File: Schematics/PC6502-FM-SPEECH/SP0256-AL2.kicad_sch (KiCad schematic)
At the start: 16 parts, among them U5 SP0256-AL2, U6 MCP6002-xSN, X2 CXO_DIP8

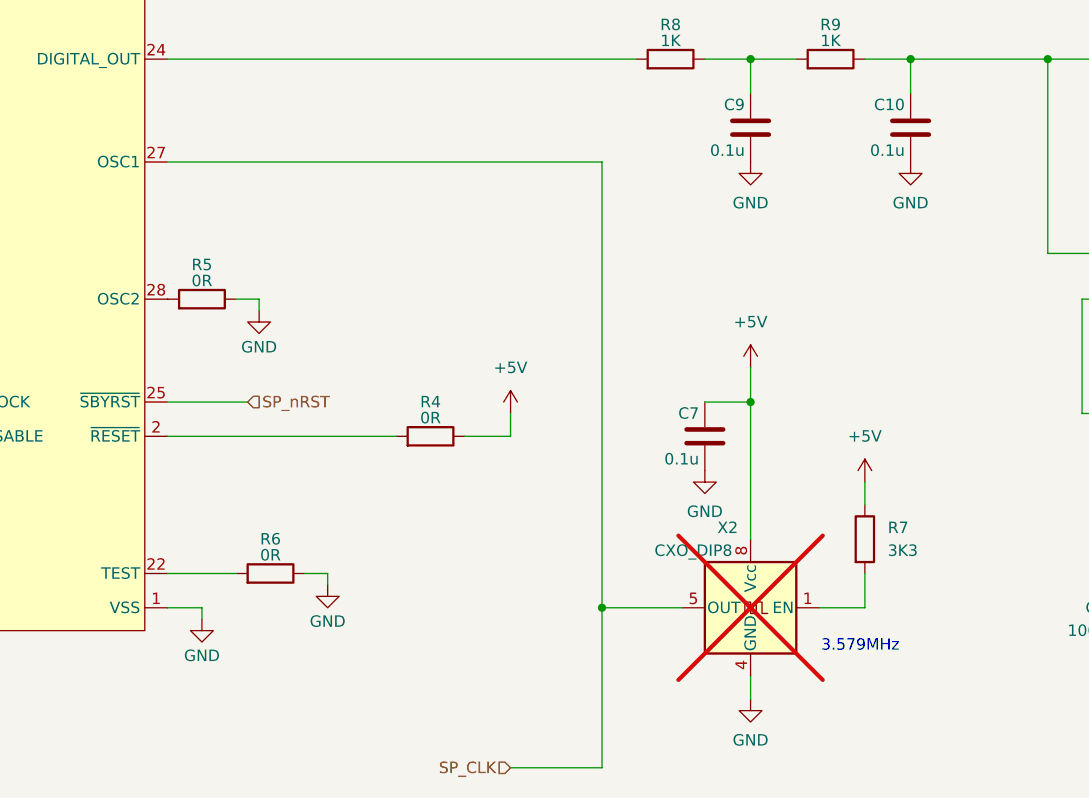
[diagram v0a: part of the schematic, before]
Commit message: Ordered Storage, FM/Speech, Dual SPI and APPLE II slot PCBs
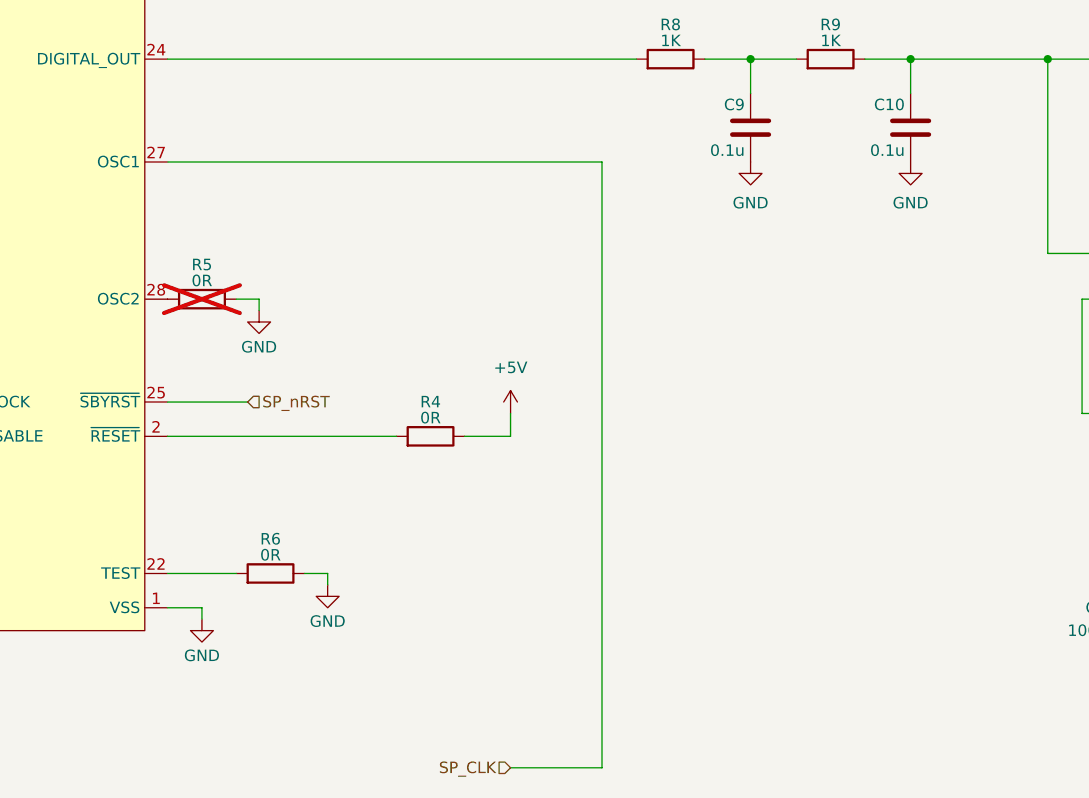
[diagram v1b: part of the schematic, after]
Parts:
- removed C7: 0.1u, Capacitor_SMD:C_0603_1608Metric, symbol Device:C
- removed R7: 3K3, Resistor_SMD:R_0603_1608Metric_Pad0.98x0.95mm_HandSolder, symbol Device:R
- removed X2: CXO_DIP8, Oscillator:Oscillator_DIP-8, symbol Oscillator:CXO_DIP8
- R5: now not fitted
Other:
- note removed: "3.579MHz"

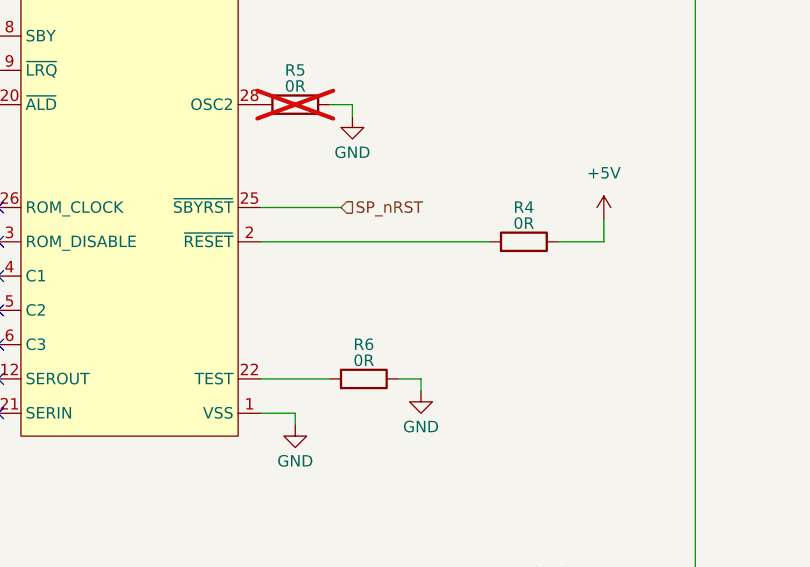
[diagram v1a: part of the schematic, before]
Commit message: SP0256 Speech synth working
SP0256 now working, couple of extra wires needed, but PCB and schematics updated.
Test code (SP0256_TEST3.BAS) created.
CPLD updated.
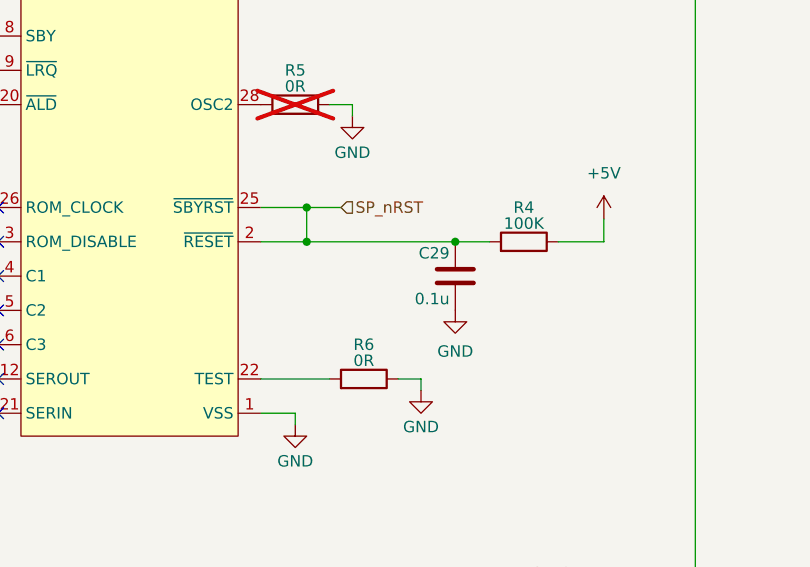
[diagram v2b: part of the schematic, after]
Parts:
- added C29: 0.1u, Capacitor_SMD:C_0603_1608Metric, symbol Device:C
- R4: value 0R -> 100K
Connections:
- net GND: now also C29.2
- net SP_nRST: now also R4.2, U5.2 (~{RESET}), C29.1
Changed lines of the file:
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@@
+	)
+	(junction
+		(at 110.49 113.03)
+		(diameter 0)
+		(color 0 0 0 0)
 	)
 	(junction
@@
 	)
 	(junction
+		(at 110.49 116.84)
+		(diameter 0)
+		(color 0 0 0 0)
+	)
+	(junction
 		(at 121.92 59.69)
 		(diameter 0)
@@
 	)
 	(junction
+		(at 127 116.84)
+		(diameter 0)
+		(color 0 0 0 0)
+	)
+	(junction
 		(at 187.96 74.93)
 		(diameter 0)
@@
 	(wire
 		(pts
+			(xy 110.49 113.03) (xy 110.49 116.84)
+		)
+		(stroke
+			(width 0)
+			(type default)
+		)
+	)
+	(wire
+		(pts
 			(xy 165.1 74.93) (xy 170.18 74.93)
 		)
@@
 	(wire
 		(pts
+			(xy 127 116.84) (xy 130.81 116.84)
+		)
+		(stroke
+			(width 0)
+			(type default)
+		)
+	)
+	(wire
+		(pts
 			(xy 214.63 125.73) (xy 214.63 128.27)
 		)
@@
 	(wire
 		(pts
+			(xy 110.49 116.84) (xy 127 116.84)
+		)
+		(stroke
+			(width 0)
+			(type default)
+		)
+	)
+	(wire
+		(pts
 			(xy 52.07 63.5) (xy 76.2 63.5)
 		)
@@
 	(wire
 		(pts
+			(xy 110.49 113.03) (xy 114.3 113.03)
+		)
+		(stroke
+			(width 0)
+			(type default)
+		)
+	)
+	(wire
+		(pts
 			(xy 143.51 153.67) (xy 153.67 153.67)
 		)
@@
 	(wire
 		(pts
-			(xy 105.41 116.84) (xy 130.81 116.84)
+			(xy 105.41 116.84) (xy 110.49 116.84)
 		)
 		(stroke
@@
 	(wire
 		(pts
-			(xy 105.41 113.03) (xy 114.3 113.03)
+			(xy 105.41 113.03) (xy 110.49 113.03)
 		)
 		(stroke
@@
 	)
 	(symbol
+		(lib_id "power:GND")
+		(at 127 124.46 0)
+		(mirror y)
+		(unit 1)
+		(exclude_from_sim no)
+		(in_bom yes)
+		(on_board yes)
+		(dnp no)
+		(fields_autoplaced yes)
+		(property "Reference" "#PWR065"
+			(at 127 130.81 0)
+			(effects
+				(font
+					(size 1.27 1.27)
+				)
+				(hide yes)
+			)
+		)
+		(property "Value" "GND"
+			(at 127 129.0225 0)
+			(effects
+				(font
+					(size 1.27 1.27)
+				)
+			)
+		)
+		(property "Footprint" ""
+			(at 127 124.46 0)
+			(effects
+				(font
+					(size 1.27 1.27)
+				)
+				(hide yes)
+			)
+		)
+		(property "Datasheet" ""
+			(at 127 124.46 0)
+			(effects
+				(font
+					(size 1.27 1.27)
+				)
+				(hide yes)
+			)
+		)
+		(property "Description" ""
+			(at 127 124.46 0)
+			(effects
+				(font
+					(size 1.27 1.27)
+				)
+			)
+		)
+		(pin "1"
+		)
+		(instances
+			(project "PC6502-FM-SPEECH"
+				(path "/431ed1ef-9b76-40e5-9f99-258de85faf41/f76dd0b6-8d4f-4054-8a53-13f969db2124"
+					(reference "#PWR065")
+					(unit 1)
+				)
+			)
+		)
+	)
+	(symbol
 		(lib_id "power:+5V")
 		(at 214.63 125.73 0)
@@
 			)
 		)
-		(property "Value" "0R"
+		(property "Value" "100K"
 			(at 134.62 114.808 90)
 			(effects
@@
 					(unit 1)
 				)
+			)
+		)
+	)
+	(symbol
+		(lib_id "Device:C")
+		(at 127 120.65 0)
+		(mirror y)
+		(unit 1)
+		(exclude_from_sim no)
+		(in_bom yes)
+		(on_board yes)
+		(dnp no)
+		(property "Reference" "C29"
+			(at 126.365 118.11 0)
+			(effects
+				(font
+					(size 1.27 1.27)
+				)
+				(justify left)
+			)
+		)
+		(property "Value" "0.1u"
+			(at 126.365 123.19 0)
+			(effects
+				(font
+					(size 1.27 1.27)
+				)
+				(justify left)
+			)
+		)
+		(property "Footprint" "Capacitor_SMD:C_0603_1608Metric"
+			(at 126.0348 124.46 0)
+			(effects
+				(font
+					(size 1.27 1.27)
+				)
+				(hide yes)
+			)
+		)
+		(property "Datasheet" "~"
+			(at 127 120.65 0)
+			(effects
+				(font
+					(size 1.27 1.27)
+				)
+				(hide yes)
+			)
+		)
+		(property "Description" ""
+			(at 127 120.65 0)
+			(effects
+				(font
+					(size 1.27 1.27)
+				)
+			)
+		)
+		(property "ManufacturerPN" "C0603C104K3RAC7867"
+			(at 127 120.65 0)
+			(effects
+				(font
+					(size 1.524 1.524)
+				)
+				(hide yes)
+			)
+		)
+		(property "Manufacturer" "Kemet"
+			(at 127 120.65 0)
+			(effects
+				(font
+					(size 1.524 1.524)
+				)
+				(hide yes)
+			)
+		)
+		(property "LCSC" ""
+			(at 127 120.65 0)
+			(effects
+				(font
+					(size 1.27 1.27)
+				)
+				(hide yes)
+			)
+		)
+		(pin "1"
+		)
+		(pin "2"
+		)
+		(instances
+			(project "PC6502-FM-SPEECH"
+				(path "/431ed1ef-9b76-40e5-9f99-258de85faf41/f76dd0b6-8d4f-4054-8a53-13f969db2124"
+					(reference "C29")
+					(unit 1)
+				)
